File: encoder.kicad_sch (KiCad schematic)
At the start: 10 parts, among them SW301 RotaryEncoder_Switch_MP

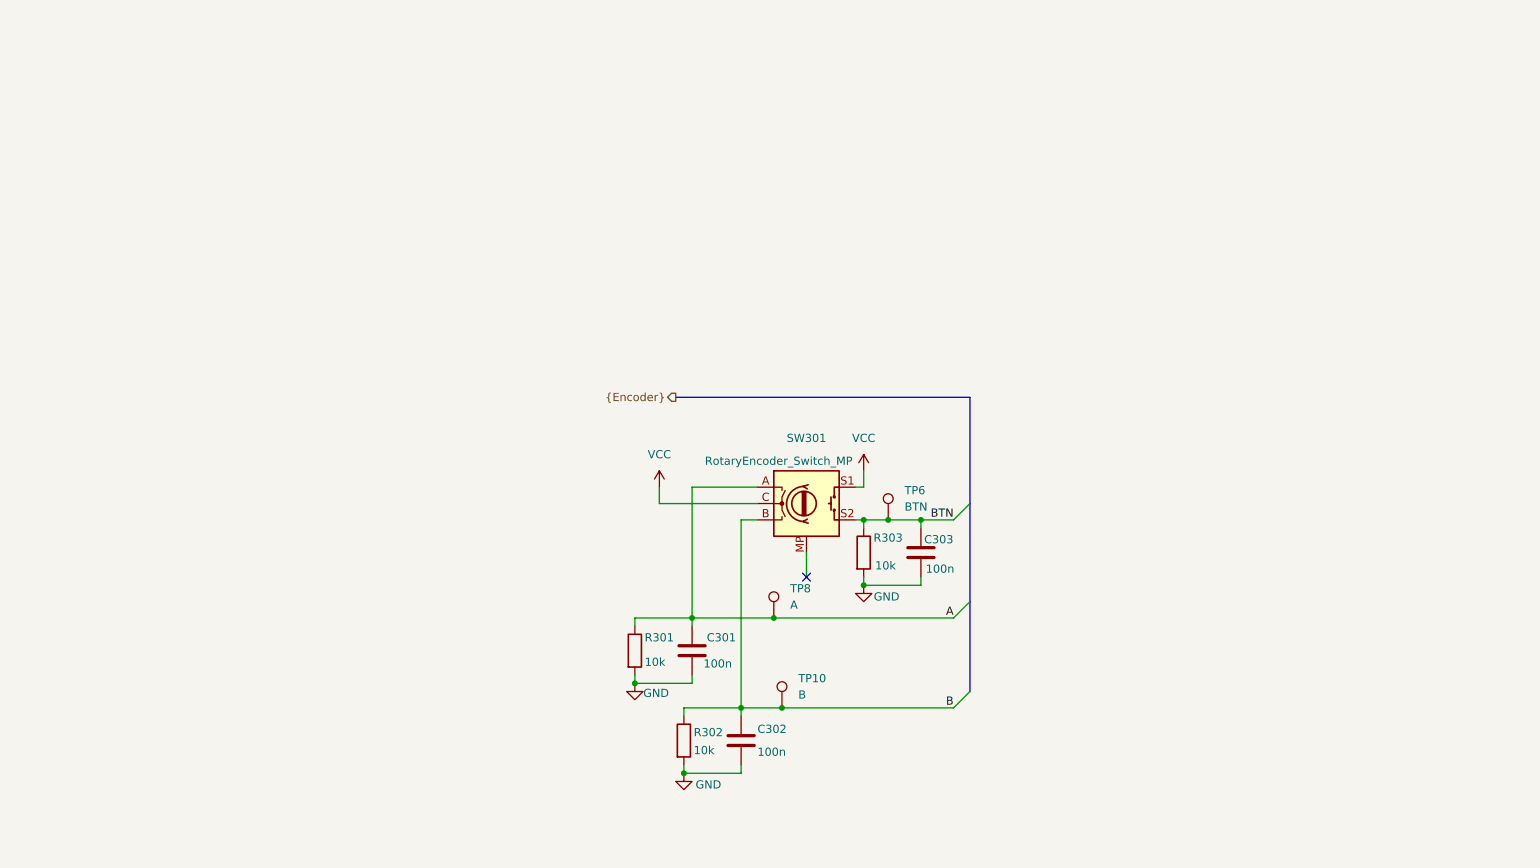
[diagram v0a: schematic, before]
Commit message: Using Schmitt trigger for encoder debouncing
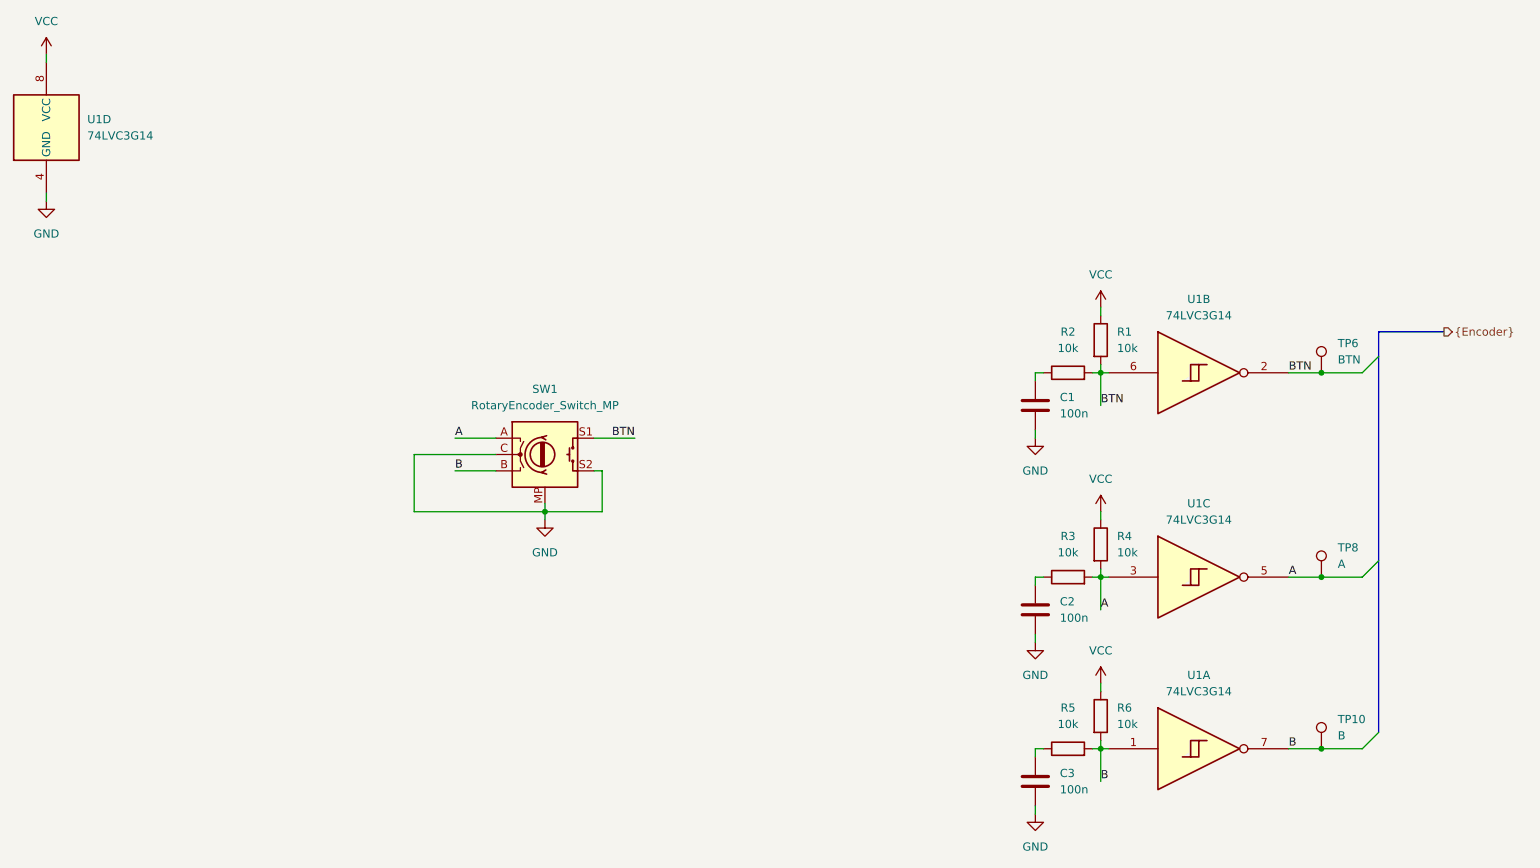
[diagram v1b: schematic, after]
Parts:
- removed C301, C302, C303: 100n, Capacitor_SMD:C_1206_3216Metric_Pad1.33x1.80mm_HandSolder, symbol Device:C
- removed R301, R302, R303: 10k, Resistor_SMD:R_1206_3216Metric_Pad1.30x1.75mm_HandSolder, symbol Device:R
- removed SW301: RotaryEncoder_Switch_MP, Rotary_Encoder:RotaryEncoder_Alps_EC12E-Switch_Vertical_H20mm, symbol Device:RotaryEncoder_Switch_MP
- added C1, C2, C3: 100n, Capacitor_SMD:C_1206_3216Metric_Pad1.33x1.80mm_HandSolder, symbol Device:C
- added R1, R2, R3, R4, R5, R6: 10k, Resistor_SMD:R_1206_3216Metric_Pad1.30x1.75mm_HandSolder, symbol Device:R
- added SW1: RotaryEncoder_Switch_MP, Rotary_Encoder:RotaryEncoder_Alps_EC12E-Switch_Vertical_H20mm, symbol Device:RotaryEncoder_Switch_MP
- added U1: 74LVC3G14, Package_SO:SSOP-8_3.9x5.05mm_P1.27mm, symbol 74xGxx:74LVC3G14
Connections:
- net A: now also R3.2, R4.2, SW1.A, U1.3, U1.5
- net B: now also R5.2, R6.2, SW1.B, U1.1, U1.7
- net BTN: now also R1.2, R2.2, SW1.S1, U1.2, U1.6
- net GND: now also C1.2, C2.2, C3.2, SW1.C, SW1.MP, SW1.S2, U1.4 (GND)
- net VCC: now also R1.1, R4.1, R6.1, U1.8 (VCC)
- new net: C3.1, R5.1
- new net: C2.1, R3.1
- new net: C1.1, R2.1
- no-connect marks 1 -> 0

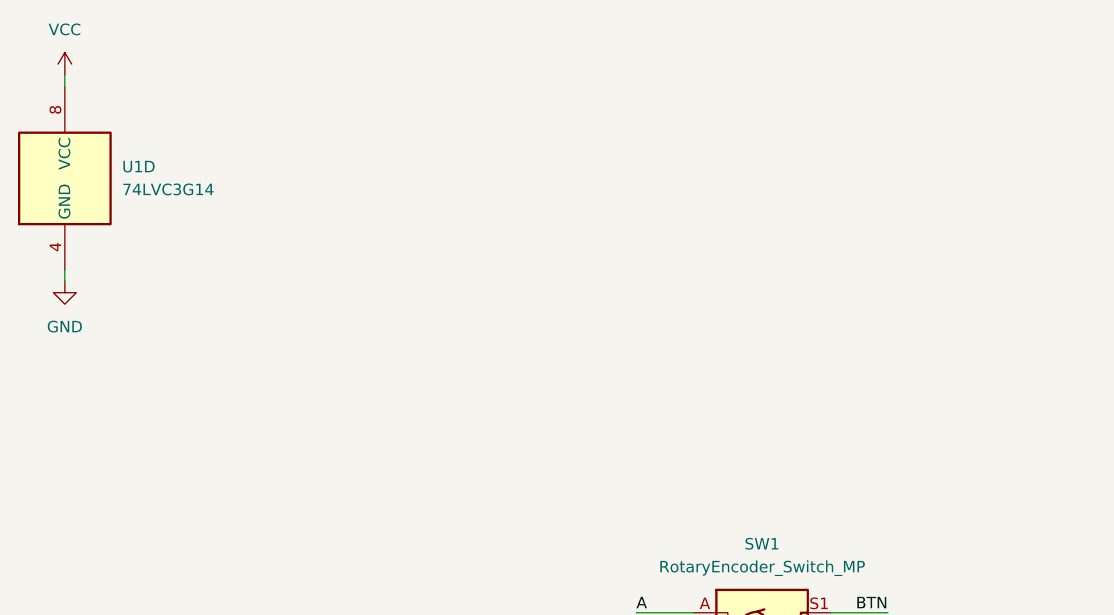
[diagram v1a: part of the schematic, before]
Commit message: Add decoupling capacitor to Schmitt trigger
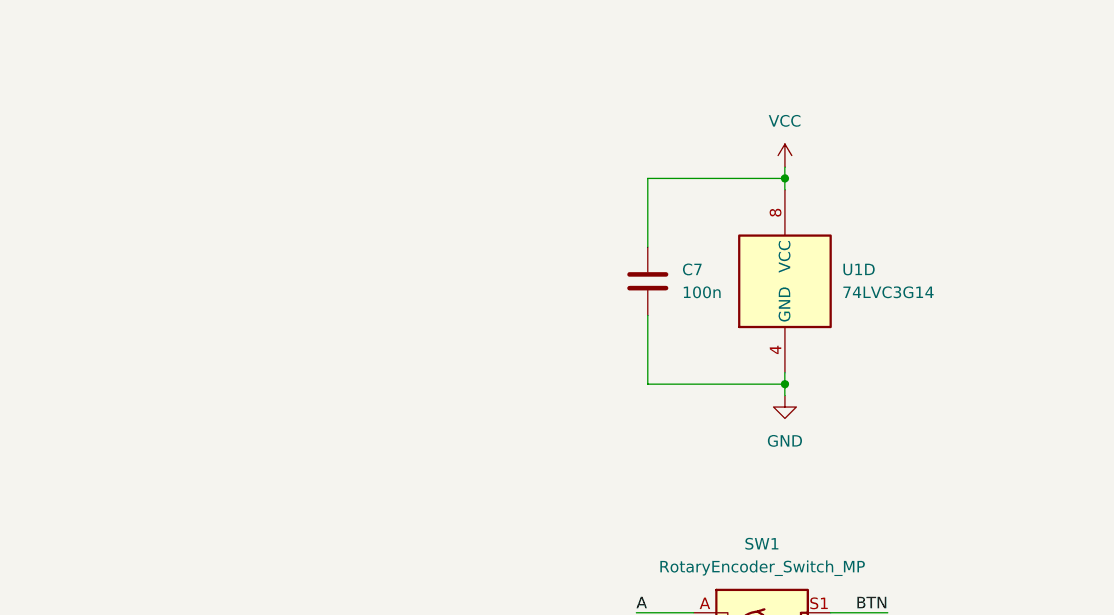
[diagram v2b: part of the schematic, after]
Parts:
- added C7: 100n, Capacitor_SMD:C_1206_3216Metric_Pad1.33x1.80mm_HandSolder, symbol Device:C
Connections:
- net GND: now also C7.2
- net VCC: now also C7.1
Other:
- moved on the sheet: U1D
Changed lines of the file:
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@@
+	)
+	(junction
+		(at 104.14 33.02)
+		(diameter 0)
+		(color 0 0 0 0)
 	)
 	(junction
@@
 	)
 	(junction
+		(at 104.14 55.88)
+		(diameter 0)
+		(color 0 0 0 0)
+	)
+	(junction
 		(at 187.96 129.54)
 		(diameter 0)
@@
 	(wire
 		(pts
+			(xy 88.9 40.64) (xy 88.9 33.02)
+		)
+		(stroke
+			(width 0)
+			(type default)
+		)
+	)
+	(wire
+		(pts
 			(xy 186.69 102.87) (xy 187.96 102.87)
 		)
@@
 	(wire
 		(pts
+			(xy 88.9 55.88) (xy 104.14 55.88)
+		)
+		(stroke
+			(width 0)
+			(type default)
+		)
+	)
+	(wire
+		(pts
+			(xy 104.14 33.02) (xy 104.14 34.29)
+		)
+		(stroke
+			(width 0)
+			(type default)
+		)
+	)
+	(wire
+		(pts
 			(xy 187.96 119.38) (xy 187.96 120.65)
 		)
@@
 	(wire
 		(pts
+			(xy 88.9 33.02) (xy 104.14 33.02)
+		)
+		(stroke
+			(width 0)
+			(type default)
+		)
+	)
+	(wire
+		(pts
 			(xy 177.8 71.12) (xy 177.8 72.39)
 		)
@@
 	(wire
 		(pts
-			(xy 24.13 21.59) (xy 24.13 22.86)
-		)
-		(stroke
-			(width 0)
-			(type default)
-		)
-	)
-	(wire
-		(pts
-			(xy 24.13 43.18) (xy 24.13 44.45)
+			(xy 104.14 31.75) (xy 104.14 33.02)
+		)
+		(stroke
+			(width 0)
+			(type default)
+		)
+	)
+	(wire
+		(pts
+			(xy 104.14 54.61) (xy 104.14 55.88)
 		)
 		(stroke
@@
 	(wire
 		(pts
+			(xy 88.9 48.26) (xy 88.9 55.88)
+		)
+		(stroke
+			(width 0)
+			(type default)
+		)
+	)
+	(wire
+		(pts
 			(xy 110.49 86.36) (xy 110.49 92.71)
 		)
@@
 		(pts
 			(xy 187.96 102.87) (xy 187.96 107.95)
+		)
+		(stroke
+			(width 0)
+			(type default)
+		)
+	)
+	(wire
+		(pts
+			(xy 104.14 55.88) (xy 104.14 57.15)
 		)
 		(stroke
@@
 	(symbol
 		(lib_id "74xGxx:74LVC3G14")
-		(at 24.13 33.02 0)
+		(at 104.14 44.45 0)
 		(unit 4)
 		(exclude_from_sim no)
@@
 		(fields_autoplaced yes)
 		(property "Reference" "U1"
-			(at 30.48 31.7499 0)
+			(at 110.49 43.1799 0)
 			(effects
 				(font
@@
 		)
 		(property "Value" "74LVC3G14"
-			(at 30.48 34.2899 0)
+			(at 110.49 45.7199 0)
 			(effects
 				(font
@@
 		)
 		(property "Footprint" "Package_SO:SSOP-8_3.9x5.05mm_P1.27mm"
-			(at 22.86 33.02 0)
+			(at 102.87 44.45 0)
 			(effects
 				(font
@@
 		)
 		(property "Datasheet" "https://www.ti.com/lit/ds/symlink/sn74lvc3g14.pdf"
-			(at 24.13 33.02 0)
+			(at 104.14 44.45 0)
 			(effects
 				(font
@@
 		)
 		(property "Description" "Triple NOT Gate Schmitt, Low-Voltage CMOS"
-			(at 24.13 33.02 0)
+			(at 104.14 44.45 0)
 			(effects
 				(font
@@
 	(symbol
 		(lib_id "power:VCC")
-		(at 24.13 21.59 0)
+		(at 104.14 31.75 0)
 		(unit 1)
 		(exclude_from_sim no)
@@
 		(fields_autoplaced yes)
 		(property "Reference" "#PWR03"
-			(at 24.13 25.4 0)
+			(at 104.14 35.56 0)
 			(effects
 				(font
@@
 		)
 		(property "Value" "VCC"
-			(at 24.13 16.51 0)
+			(at 104.14 26.67 0)
 			(effects
 				(font
@@
 		)
 		(property "Footprint" ""
-			(at 24.13 21.59 0)
+			(at 104.14 31.75 0)
 			(effects
 				(font
@@
 		)
 		(property "Datasheet" ""
-			(at 24.13 21.59 0)
+			(at 104.14 31.75 0)
 			(effects
 				(font
@@
 		)
 		(property "Description" "Power symbol creates a global label with name \"VCC\""
-			(at 24.13 21.59 0)
+			(at 104.14 31.75 0)
 			(effects
 				(font
@@
 	)
 	(symbol
+		(lib_id "Device:C")
+		(at 88.9 44.45 0)
+		(unit 1)
+		(exclude_from_sim no)
+		(in_bom yes)
+		(on_board yes)
+		(dnp no)
+		(fields_autoplaced yes)
+		(property "Reference" "C7"
+			(at 92.71 43.1799 0)
+			(effects
+				(font
+					(size 1.27 1.27)
+				)
+				(justify left)
+			)
+		)
+		(property "Value" "100n"
+			(at 92.71 45.7199 0)
+			(effects
+				(font
+					(size 1.27 1.27)
+				)
+				(justify left)
+			)
+		)
+		(property "Footprint" "Capacitor_SMD:C_1206_3216Metric_Pad1.33x1.80mm_HandSolder"
+			(at 89.8652 48.26 0)
+			(effects
+				(font
+					(size 1.27 1.27)
+				)
+				(hide yes)
+			)
+		)
+		(property "Datasheet" "~"
+			(at 88.9 44.45 0)
+			(effects
+				(font
+					(size 1.27 1.27)
+				)
+				(hide yes)
+			)
+		)
+		(property "Description" "Unpolarized capacitor"
+			(at 88.9 44.45 0)
+			(effects
+				(font
+					(size 1.27 1.27)
+				)
+				(hide yes)
+			)
+		)
+		(pin "2"
+		)
+		(pin "1"
+		)
+		(instances
+			(project "LifeCounter"
+				(path "/16b3e55a-9d75-49bf-a6fe-25414eb3d7da/8ab23184-7a75-4d74-a7c3-8fc56a0d6372"
+					(reference "C8")
+					(unit 1)
+				)
+				(path "/16b3e55a-9d75-49bf-a6fe-25414eb3d7da/e24d82de-f0b3-40eb-9854-28ed19ab91cc"
+					(reference "C7")
+					(unit 1)
+				)
+			)
+		)
+	)
+	(symbol
 		(lib_id "power:GND")
 		(at 177.8 113.03 0)
@@
 	(symbol
 		(lib_id "power:GND")
-		(at 24.13 44.45 0)
+		(at 104.14 57.15 0)
 		(unit 1)
 		(exclude_from_sim no)
@@
 		(fields_autoplaced yes)
 		(property "Reference" "#PWR04"
-			(at 24.13 50.8 0)
+			(at 104.14 63.5 0)
 			(effects
 				(font
@@
 		)
 		(property "Value" "GND"
-			(at 24.13 49.53 0)
+			(at 104.14 62.23 0)
 			(effects
 				(font
@@
 		)
 		(property "Footprint" ""
-			(at 24.13 44.45 0)
+			(at 104.14 57.15 0)
 			(effects
 				(font
@@
 		)
 		(property "Datasheet" ""
-			(at 24.13 44.45 0)
+			(at 104.14 57.15 0)
 			(effects
 				(font
@@
 		)
 		(property "Description" "Power symbol creates a global label with name \"GND\" , ground"
-			(at 24.13 44.45 0)
-			(effects
-				(font
+			(at 104.14 57.15 0)
+			(effects
+				(font

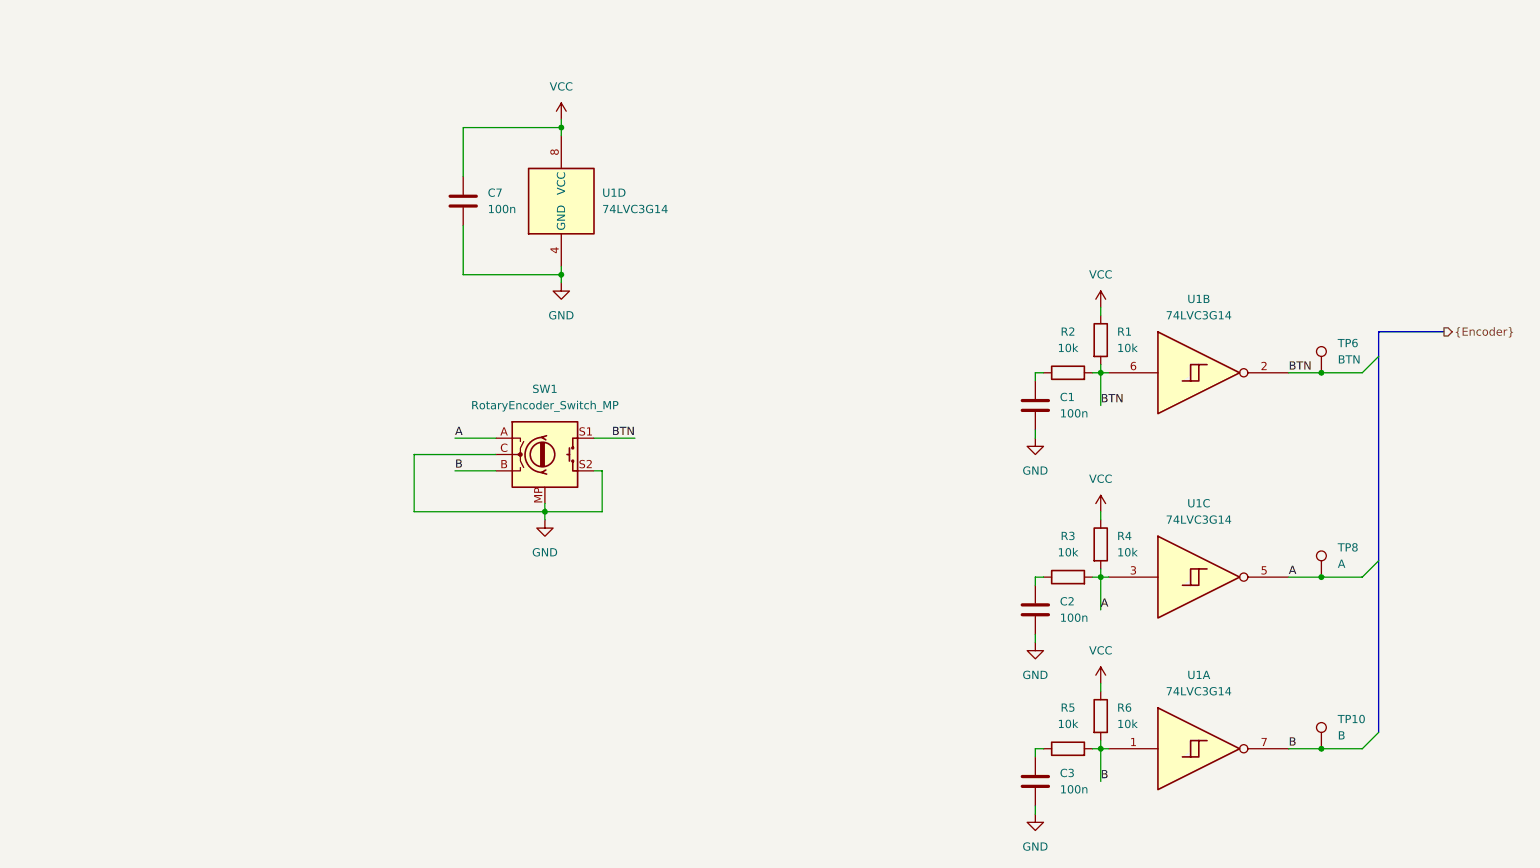
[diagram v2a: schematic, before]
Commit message: Split encoder raw and filtered signal names
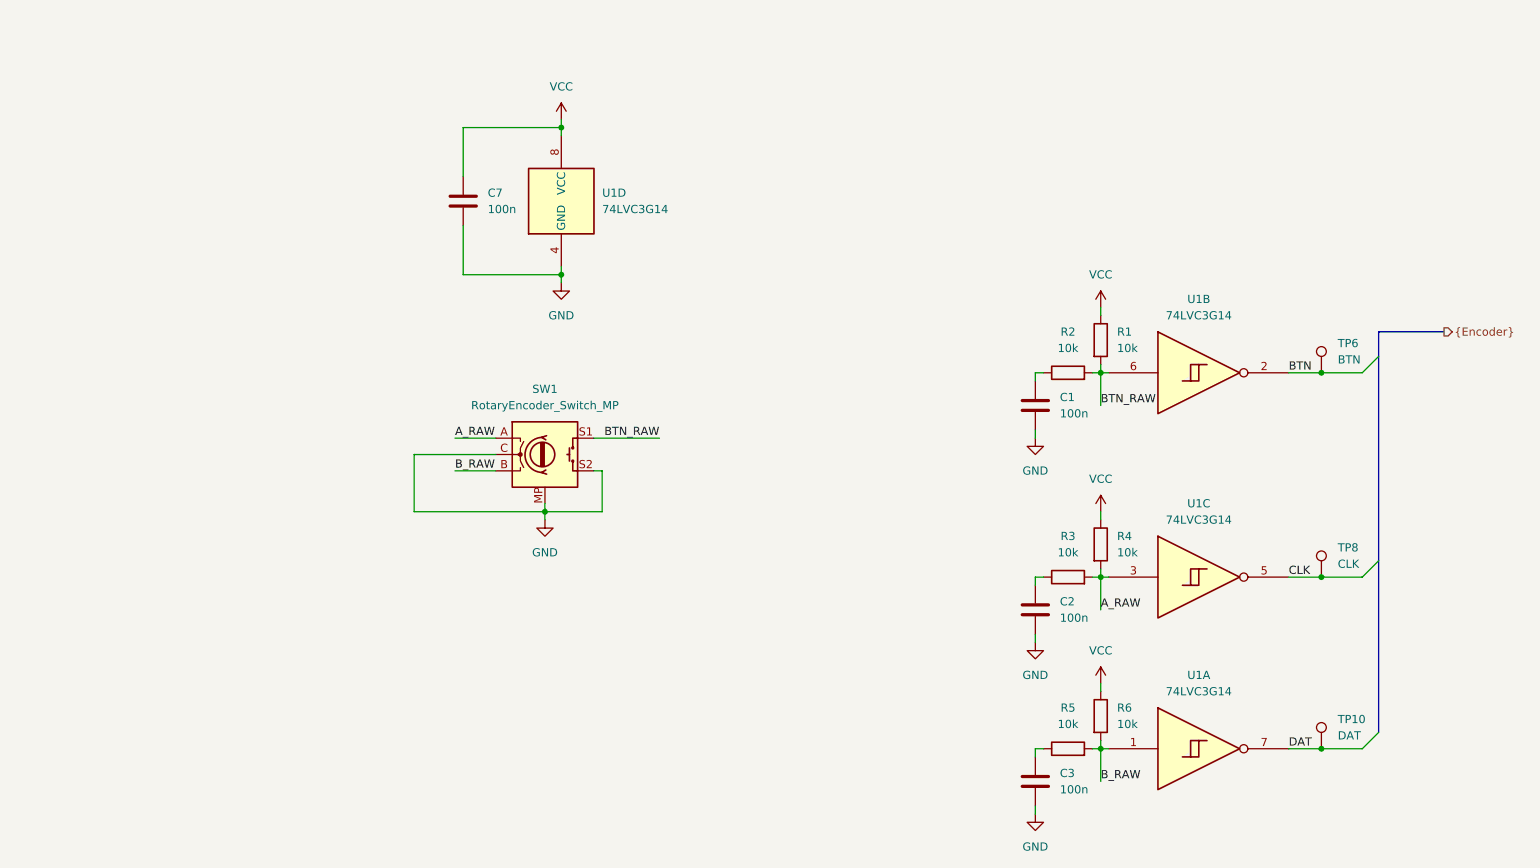
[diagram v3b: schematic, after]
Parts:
- TP10: value B -> DAT
- TP8: value A -> CLK
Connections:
- net BTN: no longer R1.2, R2.2, SW1.S1, U1.6
- net A renamed A_RAW
- net A_RAW: no longer TP8.1, U1.5
- net B renamed B_RAW
- net B_RAW: no longer TP10.1, U1.7
- new net BTN_RAW: R1.2, R2.2, SW1.S1, U1.6
- new net CLK: TP8.1, U1.5
- new net DAT: TP10.1, U1.7
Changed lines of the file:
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@@
 	(wire
 		(pts
-			(xy 109.22 81.28) (xy 115.57 81.28)
+			(xy 109.22 81.28) (xy 119.38 81.28)
 		)
 		(stroke
@@
 		)
 	)
-	(label "A"
+	(label "CLK"
 		(at 217.17 102.87 0)
 		(effects
@@
 		)
 	)
-	(label "A"
+	(label "A_RAW"
 		(at 87.63 81.28 0)
 		(effects
@@
 		)
 	)
-	(label "BTN"
-		(at 115.57 81.28 180)
+	(label "BTN_RAW"
+		(at 119.38 81.28 180)
 		(effects
 			(font
@@
 		)
 	)
-	(label "B"
+	(label "B_RAW"
 		(at 187.96 134.62 0)
 		(effects
@@
 		)
 	)
-	(label "B"
+	(label "B_RAW"
 		(at 87.63 86.36 0)
 		(effects
@@
 		)
 	)
-	(label "BTN"
+	(label "BTN_RAW"
 		(at 187.96 76.2 0)
 		(effects
@@
 		)
 	)
-	(label "B"
+	(label "DAT"
 		(at 217.17 129.54 0)
 		(effects
@@
 		)
 	)
-	(label "A"
+	(label "A_RAW"
 		(at 187.96 107.95 0)
 		(effects
@@
 			)
 		)
-		(property "Value" "A"
+		(property "Value" "CLK"
 			(at 224.79 100.8379 0)
 			(effects
@@
 			)
 		)
-		(property "Value" "B"
+		(property "Value" "DAT"
 			(at 224.79 127.5079 0)
 			(effects

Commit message: Fix encoder debounce
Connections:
- net A_RAW: no longer U1.3
- net BTN_RAW: no longer U1.6
- net B_RAW: no longer U1.1
- net at C3.1, R5.1: now also U1.1
- net at C2.1, R3.1: now also U1.3
- net at C1.1, R2.1: now also U1.6
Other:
- moved on the sheet: C1, C2, C3, C7, R1, R2, R3, R4, R5, R6, SW1, TP10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
